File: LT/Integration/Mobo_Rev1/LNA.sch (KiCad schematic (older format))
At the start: 10 parts, among them Q1 5486

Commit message: STEP files
I attempted to add as many step files into the Mother Board kicad as I could
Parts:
- C2: footprint LT:CAP_trimmer_SGC3 -> LT:CAP_trimmer_SGC3_Download
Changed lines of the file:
@@
 EESchema Schematic File Version 4
-EELAYER 30 0
+LIBS:Mobo_Rev1-cache
+EELAYER 26 0
 EELAYER END
 $Descr A4 11693 8268
@@
 F 0 "C2" H 4215 1946 50  0000 L CNN
 F 1 "SGCS" H 4215 1855 50  0000 L CNN
-F 2 "LT:CAP_trimmer_SGC3" H 4100 1900 50  0001 C CNN
+F 2 "LT:CAP_trimmer_SGC3_Download" H 4100 1900 50  0001 C CNN
 F 3 "~" H 4100 1900 50  0001 C CNN
 	1    4100 1900

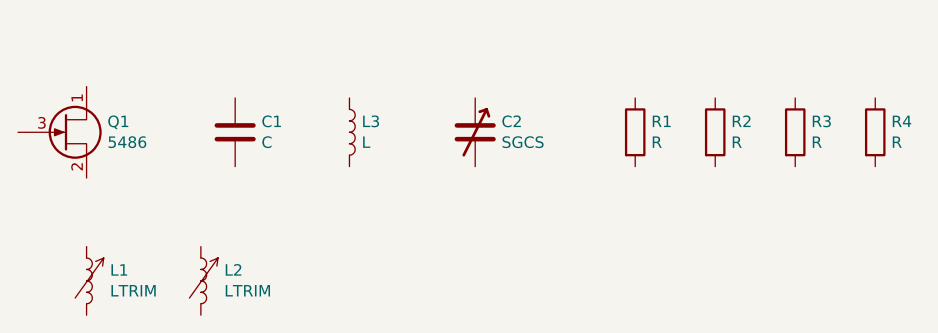
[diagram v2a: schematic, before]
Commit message: Just Testing GitBash, changed a resistor value in LNA
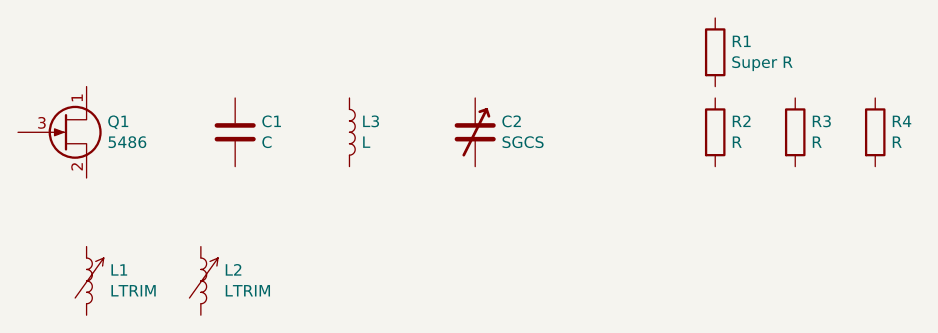
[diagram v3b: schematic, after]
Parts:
- R1: value R -> Super R
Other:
- moved on the sheet: R1
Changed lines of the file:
@@
 L Device:R R1
 U 1 1 5E4B318F
-P 4800 1900
-F 0 "R1" H 4870 1946 50  0000 L CNN
-F 1 "R" H 4870 1855 50  0000 L CNN
-F 2 "Resistor_SMD:R_0805_2012Metric" V 4730 1900 50  0001 C CNN
-F 3 "~" H 4800 1900 50  0001 C CNN
-	1    4800 1900
+P 5150 1550
+F 0 "R1" H 5220 1596 50  0000 L CNN
+F 1 "Super R" H 5220 1505 50  0000 L CNN
+F 2 "Resistor_SMD:R_0805_2012Metric" V 5080 1550 50  0001 C CNN
+F 3 "~" H 5150 1550 50  0001 C CNN
+	1    5150 1550
 	1    0    0    -1
 $EndComp
